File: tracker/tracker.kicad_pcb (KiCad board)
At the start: 2 copper layers, 1 part, among them U1 XIAO-ESP32-C6-SMD

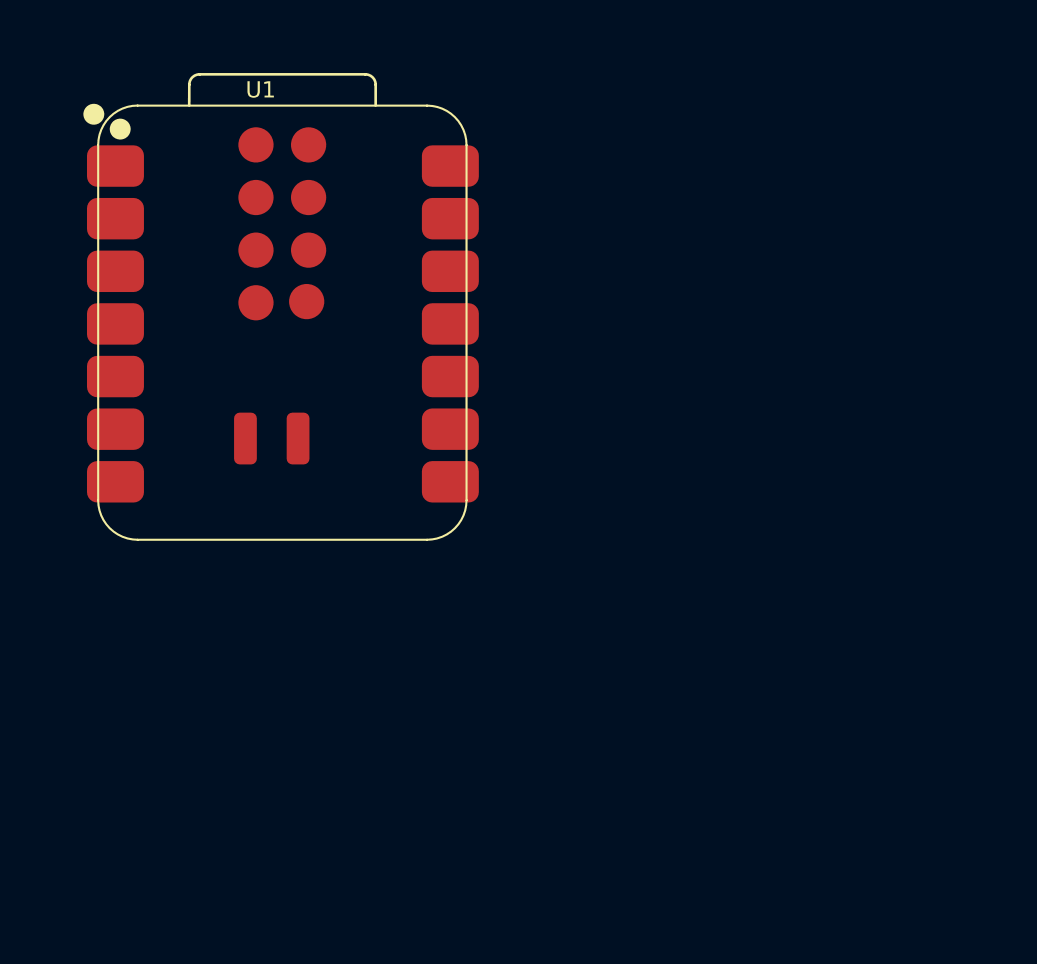
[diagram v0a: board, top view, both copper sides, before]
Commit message: adding protection , charging ic
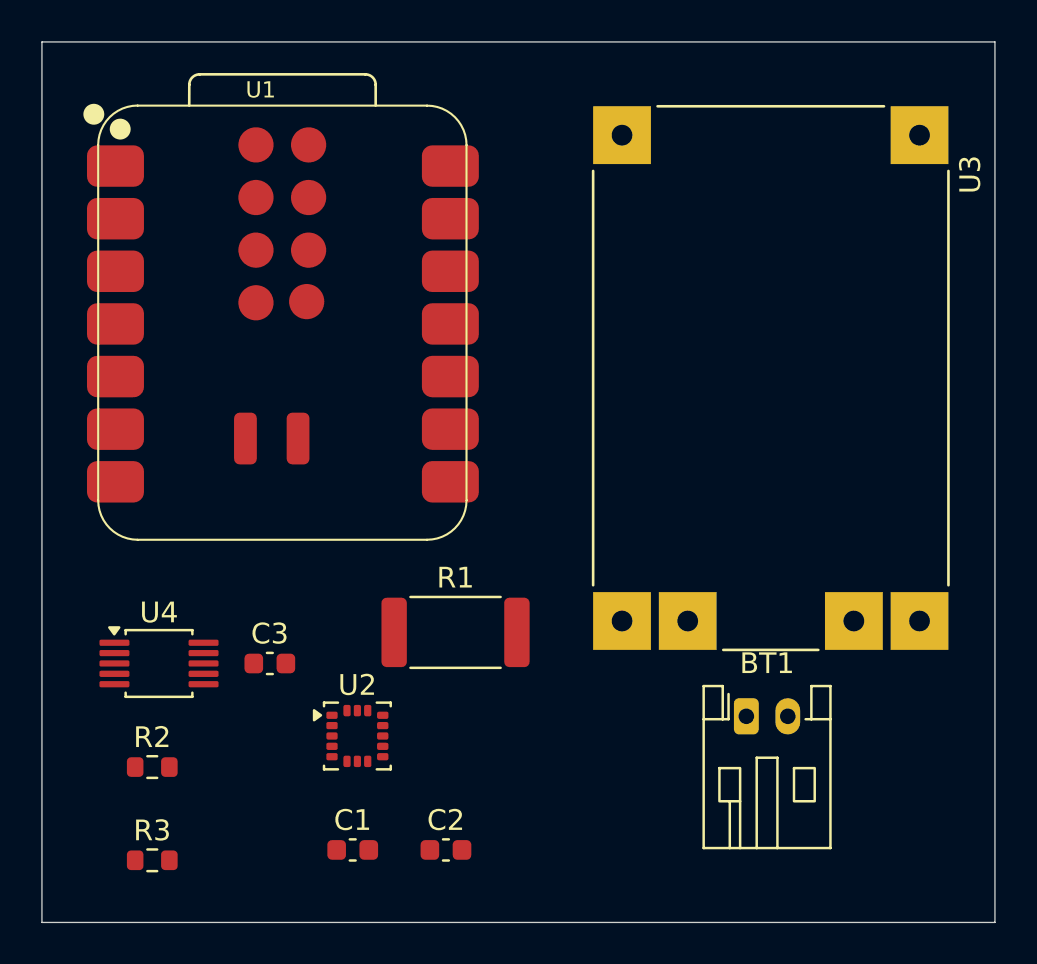
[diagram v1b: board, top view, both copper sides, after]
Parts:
- added BT1: Battery_Cell, Connector_JST:JST_PH_S2B-PH-K_1x02_P2.00mm_Horizontal, F.Cu at (144.5, 116.0)
- added C1: 100n, Capacitor_SMD:C_0603_1608Metric, F.Cu at (125.5, 122.5)
- added C2: 10u, Capacitor_SMD:C_0603_1608Metric, F.Cu at (130.0, 122.5)
- added C3: 100n, Capacitor_SMD:C_0603_1608Metric, F.Cu at (121.5, 113.5)
- added R1: 0.1, Resistor_SMD:R_2512_6332Metric, F.Cu at (130.5, 112.0)
- added R2: 4.7k, Resistor_SMD:R_0603_1608Metric, F.Cu at (115.8, 118.5)
- added R3: 4.7k, Resistor_SMD:R_0603_1608Metric, F.Cu at (115.8, 123.0)
- added U2: LIS3DH, Package_LGA:LGA-16_3x3mm_P0.5mm_LayoutBorder3x5y, F.Cu at (125.7, 117.0)
- added U3: TP4056_MICRO-USB_CHARGER_-_1A, TP4056_MICRO-USB_CHARGER_-_1A:MODULE_TP4056_MICRO-USB_CHARGER_-_1A, F.Cu at (145.7, 99.7)
- added U4: INA226AIDGSR, Package_SO:TSSOP-10_3x3mm_P0.5mm, F.Cu at (116.2, 113.5)
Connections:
- U1 pad 1: unconnected-(U1-D0-Pad1) -> Net-(U1-D0)
- U1 pad 12: unconnected-(U1-3V3_OUT-Pad12) -> Net-(U2-CS)
- U1 pad 13: unconnected-(U1-GND-Pad13) -> GND
- U1 pad 23: unconnected-(U1-VBAT-Pad23) -> Net-(U1-VBAT)
- U1 pad 24: unconnected-(U1-GND-Pad24) -> GND
- U1 pad 3: unconnected-(U1-D2-Pad3) -> Net-(U1-D2)
- U1 pad 5: unconnected-(U1-D4-Pad5) -> Net-(U1-D4)
- U1 pad 6: unconnected-(U1-D5-Pad6) -> Net-(U1-D5)
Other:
- board outline added: 46 x 42.5 mm

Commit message: friday update
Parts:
- added C5: 10u, Capacitor_SMD:C_0603_1608Metric, F.Cu at (136.0, 86.3)
- added C6: 10u, Capacitor_SMD:C_0603_1608Metric, F.Cu at (136.0, 88.8)
- added C7: 100n, Capacitor_SMD:C_0603_1608Metric, F.Cu at (136.0, 91.3)
- added J1: USB_C_Receptacle_PowerOnly_6P, Package_DFN_QFN:QFN-24-1EP_4x4mm_P0.5mm_EP2.7x2.7mm, F.Cu at (142.5, 87.2)
- added Q1: DMG9926UDM-7, dikigey_dual_channel_nfets:SOT-26_DIO, F.Cu at (142.6, 101.5)
- added R4: 2.4k, Resistor_SMD:R_0603_1608Metric, F.Cu at (136.0, 93.8)
- added R5: 5.1k, Resistor_SMD:R_0603_1608Metric, F.Cu at (136.0, 96.3)
- added R6: 5.1k, Resistor_SMD:R_0603_1608Metric, F.Cu at (136.0, 98.8)
- added R7: 100, Resistor_SMD:R_0603_1608Metric, F.Cu at (136.0, 101.3)
- added R9: 1k, Resistor_SMD:R_0603_1608Metric, F.Cu at (136.0, 103.8)
- added U5: TP4056-42-ESOP8, Package_SO:SOIC-8-1EP_3.9x4.9mm_P1.27mm_EP2.41x3.3mm_ThermalVias, F.Cu at (143.7, 95.2)
- U3: value TP4056_MICRO-USB_CHARGER_-_1A -> DW01A; footprint TP4056_MICRO-USB_CHARGER_-_1A:MODULE_TP4056_MICRO-USB_CHARGER_-_1A -> Package_TO_SOT_SMD:SOT-23-6
- moved U3 6.28 mm to (146.0, 106.0)
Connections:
- BT1 pad 1: Net-(BT1-+) -> /Charging_and_Battery/BAT+
- BT1 pad 2: Net-(BT1--) -> /Charging_and_Battery/BAT-
- R1 pad 1: Net-(U3-OUT+) -> /Charging_and_Battery/BAT+
- U4 pad 10: Net-(U3-OUT+) -> /Charging_and_Battery/BAT+
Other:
- board size 46 x 42.5 mm -> 40 x 42.5 mm

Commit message: added led's
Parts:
- added D1: LED, LED_SMD:LED_0603_1608Metric, F.Cu at (143.7, 106.9)
- added D2: LED, LED_SMD:LED_0603_1608Metric, F.Cu at (143.7, 109.5)
- added R10: 680, Resistor_SMD:R_0603_1608Metric, F.Cu at (147.7, 109.4)
- added R8: 680, Resistor_SMD:R_0603_1608Metric, F.Cu at (147.7, 106.9)
- J1: footprint Package_DFN_QFN:QFN-24-1EP_4x4mm_P0.5mm_EP2.7x2.7mm -> Connector_USB:USB_C_Receptacle_HRO_TYPE-C-31-M-12
- R4: value 2.4k -> 1.2k
- U4: footprint Package_SO:TSSOP-10_3x3mm_P0.5mm -> Package_SO:MSOP-10_3x3mm_P0.5mm
- moved U1 32.9 mm to (129.5, 79.0), turned to 180 degrees
- moved Q1 18.3 mm to (134.9, 118.0)
- moved R1 15.3 mm to (116.0, 107.0)
- moved U3 9.01 mm to (138.5, 111.0)
- moved U5 4.21 mm to (144.0, 99.4)
- moved BT1 2.92 mm to (142.0, 117.5)
- moved J1 2.23 mm to (143.5, 89.2), turned to -90 degrees
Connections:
- net Net-(U1-VBAT) renamed /Shunt_Output
- U5 pad 6: unconnected-(U5-~{STDBY}-Pad6) -> Net-(D2-K)
- U5 pad 7: unconnected-(U5-~{CHRG}-Pad7) -> Net-(D1-K)
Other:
- board size 40 x 42.5 mm -> 40 x 50.5 mm

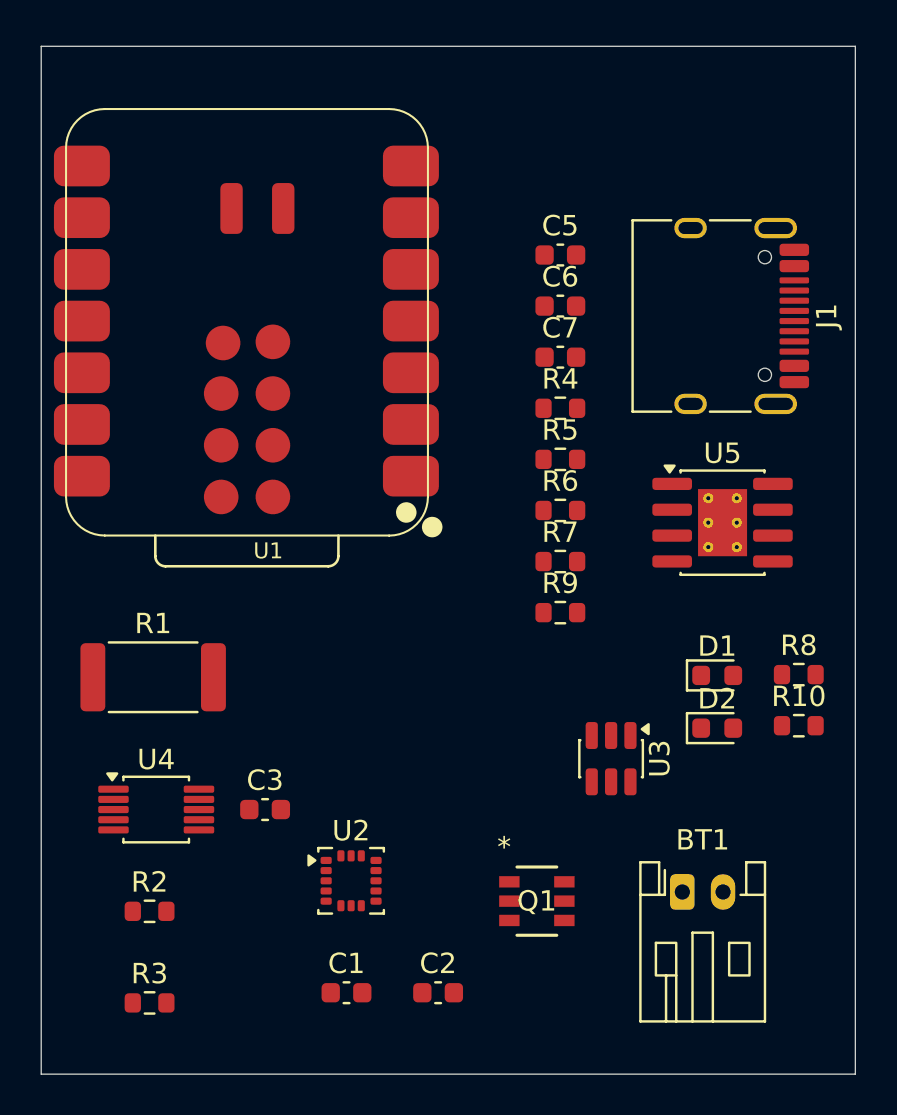
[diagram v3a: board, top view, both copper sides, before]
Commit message: started routing
i can do this , 2 planes easy peasy
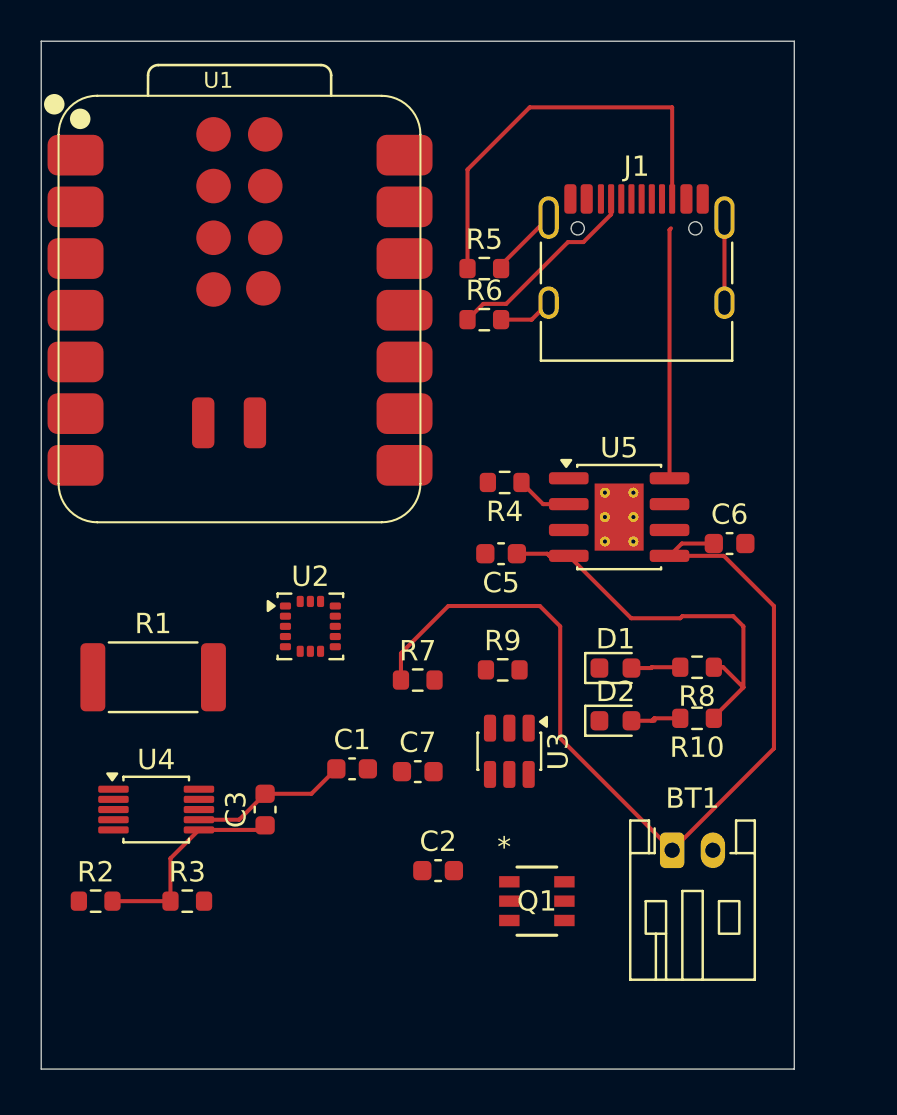
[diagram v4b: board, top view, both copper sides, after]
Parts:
- moved U1 27.4 mm to (111.4, 99.5), turned to 0 degrees
- moved C7 21.5 mm to (129.0, 111.6)
- moved C5 15.0 mm to (133.1, 100.9), turned to 180 degrees
- moved C6 14.3 mm to (144.3, 100.4)
- moved U2 12.7 mm to (123.7, 104.5)
- moved C1 11.0 mm to (125.8, 111.5)
- moved R5 10.1 mm to (132.3, 86.9)
- moved R6 10.1 mm to (132.3, 89.4)
- moved R7 9.11 mm to (129.0, 107.1)
- moved C2 6.00 mm to (130.0, 116.5)
- moved R3 5.33 mm to (117.7, 118.0)
- moved U5 5.09 mm to (138.9, 99.1)
- moved R8 5.01 mm to (142.7, 106.5), turned to 180 degrees
- moved D1 5.01 mm to (138.7, 106.5)
- moved D2 5.01 mm to (138.7, 109.1)
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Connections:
- R10 pad 1: GND -> Net-(U5-CE)
- R8 pad 1: GND -> Net-(U5-CE)
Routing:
- net /Charging_and_Battery/BAT+: track 0.00 -> 46.4 mm
- net Net-(U5-CE): track 0.00 -> 32.0 mm
- net Net-(J1-CC2): track 0.00 -> 20.7 mm
- net GND: track 0.00 -> 18.1 mm
- net Net-(U2-CS): track 0.00 -> 10.3 mm
- net Net-(J1-CC1): track 0.00 -> 9.96 mm
- net Net-(U5-PROG): track 0.00 -> 2.77 mm
- net Net-(D2-A): track 0.00 -> 2.58 mm
- net Net-(D1-A): track 0.00 -> 2.42 mm
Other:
- board size 40 x 50.5 mm -> 37 x 50.5 mm

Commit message: started pcb design
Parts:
- moved C5 60.3 mm to (188.0, 76.0)
- moved J1 49.4 mm to (188.4, 96.1)
- moved R5 49.4 mm to (181.0, 95.5)
- moved R6 49.4 mm to (181.0, 98.0)
- moved D1 41.0 mm to (170.8, 81.0)
- moved D2 41.0 mm to (170.8, 83.6)
- moved R10 41.0 mm to (174.8, 83.5)
- moved R8 41.0 mm to (174.8, 81.0)
- moved C1 33.1 mm to (92.8, 109.5)
- moved C2 33.1 mm to (97.0, 114.5)
- moved U5 26.7 mm to (159.9, 82.7)
- moved R4 24.7 mm to (152.5, 82.0)
- moved U3 24.6 mm to (157.0, 103.5), turned to 180 degrees
- moved U2 24.3 mm to (102.0, 93.7), turned to 180 degrees
- moved R9 24.2 mm to (157.0, 111.0), turned to -90 degrees
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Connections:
- net Net-(U1-D4) renamed SDA
- net Net-(U5-CE) renamed USB_VBUS
- C1 pad 1: GND -> -VSW
- C1 pad 2: Net-(U2-CS) -> 3v3
- C2 pad 1: GND -> -VSW
- C2 pad 2: Net-(U2-CS) -> 3v3
- C3 pad 1: Net-(U2-CS) -> 3v3
- C3 pad 2: GND -> -VSW
- C5 pad 2: GND -> -VSW
- C6 pad 1: /Charging_and_Battery/BAT+ -> -VSW
- C6 pad 2: GND -> /Charging_and_Battery/BAT+
- J1 pad A12: GND -> -VSW
- J1 pad B12: GND -> -VSW
- J1 pad SH: GND -> -VSW
- Q1 pad 3: GND -> -VSW
- R2 pad 1: Net-(U1-D5) -> (no net)
- R2 pad 2: Net-(U2-CS) -> (no net)
- R3 pad 1: Net-(U2-CS) -> 3v3
- R4 pad 2: GND -> -VSW
- R5 pad 2: GND -> -VSW
- R6 pad 2: GND -> -VSW
- R9 pad 2: GND -> /Charging_and_Battery/PROTECT_MID
- U1 pad 12: Net-(U2-CS) -> 3v3
- U1 pad 13: GND -> -VSW
- U1 pad 24: GND -> -VSW
- U1 pad 6: Net-(U1-D5) -> SCL
- U2 pad 1: Net-(U2-CS) -> 3v3
- U2 pad 10: GND -> -VSW
- U2 pad 12: GND -> -VSW
- U2 pad 14: Net-(U2-CS) -> 3v3
- U2 pad 4: Net-(U1-D5) -> SCL
- U2 pad 5: GND -> -VSW
- U2 pad 8: Net-(U2-CS) -> 3v3
- U4 pad 1: GND -> -VSW
- U4 pad 2: GND -> -VSW
- U4 pad 5: Net-(U1-D5) -> SCL
- U4 pad 6: Net-(U2-CS) -> 3v3
- U4 pad 7: GND -> -VSW
- U5 pad 1: GND -> -VSW
- U5 pad 3: GND -> -VSW
- U5 pad 9: GND -> -VSW
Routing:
- net 3v3: track 0.00 -> 120.7 mm, vias 0 -> 1
- net USB_VBUS: track 32.0 -> 110.4 mm, vias 0 -> 1
- net SDA: track 0.00 -> 73.4 mm, vias 0 -> 1
- net SCL: track 0.00 -> 45.8 mm
- net /Shunt_Output: track 0.00 -> 39.7 mm
- net Net-(U3-OC): track 0.00 -> 30.4 mm
- net /Charging_and_Battery/BAT-: track 0.00 -> 23.5 mm
- net Net-(U3-OD): track 0.00 -> 21.3 mm
- net GND: track 18.1 -> 0.00 mm
- net /Charging_and_Battery/PROTECT_MID: track 0.00 -> 11.0 mm
- net /Charging_and_Battery/BAT+: track 46.4 -> 57.3 mm
- net Net-(U2-CS): track 10.3 -> 0.00 mm
- net Net-(U3-VCC): track 0.00 -> 9.85 mm
- net Net-(D1-K): track 0.00 -> 8.54 mm
- net Net-(D2-K): track 0.00 -> 7.83 mm
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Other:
- board outline removed

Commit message: working on ground
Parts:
- J1: footprint Connector_USB:USB_C_Receptacle_HRO_TYPE-C-31-M-12 -> Connector_USB:USB_C_Receptacle_GCT_USB4125-xx-x-0190_6P_TopMnt_Horizontal
- moved C5 36.3 mm to (158.0, 96.5), turned to -90 degrees
- moved R5 33.6 mm to (149.0, 85.0), turned to 180 degrees
- moved R8 33.4 mm to (141.5, 80.2), turned to -90 degrees
- moved J1 32.6 mm to (156.8, 88.5)
- moved R6 32.6 mm to (149.3, 90.4), turned to 180 degrees
- moved R10 31.0 mm to (144.0, 80.2), turned to -90 degrees
- moved D1 29.5 mm to (141.5, 84.2), turned to 90 degrees
- moved D2 26.7 mm to (144.1, 84.2), turned to 90 degrees
- moved R4 22.8 mm to (142.5, 102.5), turned to -90 degrees
- moved U5 20.8 mm to (143.2, 95.1), turned to 90 degrees
- moved C1 8.94 mm to (101.2, 112.4), turned to 180 degrees
- moved C2 5.77 mm to (101.2, 118.4), turned to 180 degrees
- moved C3 5.70 mm to (119.5, 122.5)
- turned R2 to -90 degrees
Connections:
- net -VSW renamed GND
- R2 pad 1: (no net) -> SCL
- R2 pad 2: (no net) -> 3v3
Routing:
- net GND: track 4.35 -> 221.2 mm, vias 0 -> 6
- net Net-(U1-D0): track 0.00 -> 43.1 mm, vias 0 -> 2
- net (no net): track 2.67 -> 36.8 mm, vias 0 -> 1
- net Net-(U1-D2): track 0.00 -> 25.0 mm
- net /Shunt_Output: track 39.7 -> 60.8 mm, vias 0 -> 2
- net /Charging_and_Battery/BAT+: track 57.3 -> 46.2 mm
- net Net-(J1-CC2): track 20.7 -> 10.7 mm, vias 0 -> 2
- net USB_VBUS: track 110.4 -> 103.5 mm, vias 1 -> 2
- net 3v3: track 120.7 -> 113.9 mm, vias 1 -> 2
- net SDA: track 73.4 -> 67.4 mm
- net SCL: track 45.8 -> 49.0 mm, vias 0 -> 1
- net Net-(J1-CC1): track 14.9 -> 12.0 mm
- net Net-(U3-CS): track 6.86 -> 7.53 mm
- added copper zone on B.Cu, net GND
- added copper zone on F.Cu, net GND
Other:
- board outline added: 79.5 x 62.5 mm

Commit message: just i drc issue left, maybe push type c a bit forward
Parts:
- moved C1 10.5 mm to (102.2, 101.9)
- moved C2 10.5 mm to (102.2, 107.9)
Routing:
- net GND: track 221.2 -> 276.8 mm, vias 6 -> 12
- net (no net): track 36.8 -> 0.00 mm, vias 1 -> 0
- net USB_VBUS: track 103.5 -> 108.6 mm, vias 2 -> 3
- net 3v3: track 113.9 -> 111.8 mm, vias 2 -> 5
- net Net-(J1-CC2): track 10.7 -> 12.8 mm
- net SDA: track 67.4 -> 68.0 mm, vias 1 -> 3
- net SCL: track 49.0 -> 49.2 mm, vias 1 -> 2
- removed copper zone on B.Cu, net GND
- removed copper zone on F.Cu, net GND

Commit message: made pcb . bpm , cpl
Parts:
- moved J1 7.08 mm to (158.0, 81.6)
- moved C5 7.00 mm to (158.0, 89.5)
- moved Q1 6.40 mm to (158.0, 113.1)
- moved D1 4.81 mm to (142.0, 89.0)
- moved D2 4.81 mm to (144.6, 89.0)
- moved R10 4.81 mm to (144.5, 85.0)
- moved R8 4.81 mm to (142.0, 85.0)
- moved R9 2.67 mm to (157.0, 108.3)
- moved C2 2.42 mm to (102.2, 105.5)
- moved R3 1.58 mm to (104.0, 123.3)
- moved C1 0.92 mm to (102.2, 101.0)
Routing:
- net /Shunt_Output: track 60.8 -> 73.0 mm, vias 2 -> 4
- net Net-(U3-OD): track 21.3 -> 10.2 mm
- net Net-(U3-OC): track 30.4 -> 19.9 mm
- net Net-(J1-CC1): track 12.0 -> 19.1 mm
- net Net-(D1-K): track 8.54 -> 3.05 mm
- net Net-(J1-CC2): track 12.8 -> 17.7 mm
- net SDA: track 68.0 -> 63.3 mm
- net GND: track 276.8 -> 272.2 mm, vias 12 -> 15
- net Net-(D2-K): track 7.83 -> 3.67 mm
- net /Charging_and_Battery/PROTECT_MID: track 11.0 -> 7.32 mm
- net USB_VBUS: track 108.6 -> 104.9 mm, vias 3 -> 2
- net /Charging_and_Battery/BAT+: track 46.2 -> 48.9 mm
- net Net-(U3-CS): track 7.53 -> 4.86 mm
- net /Charging_and_Battery/BAT-: track 23.5 -> 25.1 mm
- net Net-(U1-D0): track 43.1 -> 41.7 mm
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- added copper zone on B.Cu, net GND
- added copper zone on F.Cu, net GND
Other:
- board size 79.5 x 62.5 mm -> 69 x 51.6 mm
